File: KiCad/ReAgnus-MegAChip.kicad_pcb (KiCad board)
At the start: 4 copper layers, 78 x 49 mm, 24 parts, among them J1 Conn_01x03, J3 Conn_02x01, J4 Conn_01x01, J5 Conn_01x01, J6 Conn_01x01, J7 Conn_01x01, U1 PLCC-84-Plug, U2 LM1117-3.3, U3 SN74CBTD16210, U4 SN74CBTD16210, U5 SN74CBTD16210, U6 SN74CBTD16210, U7 GW1N-UV9LQ144, U8 74LVC1G07, U9 Agnus_TH_plug_pins

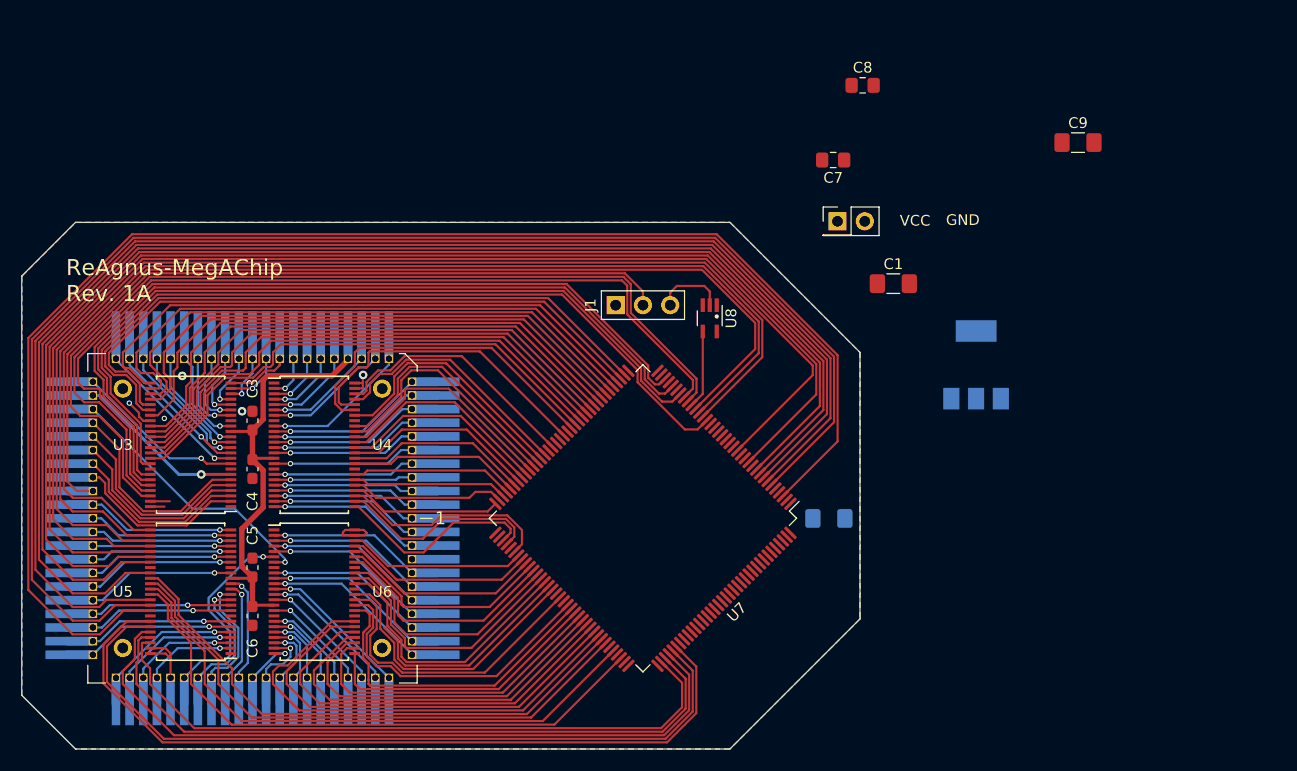
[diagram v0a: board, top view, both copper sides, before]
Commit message: added pull-up resistors on PAL/NTSC-line, added JTAG-header
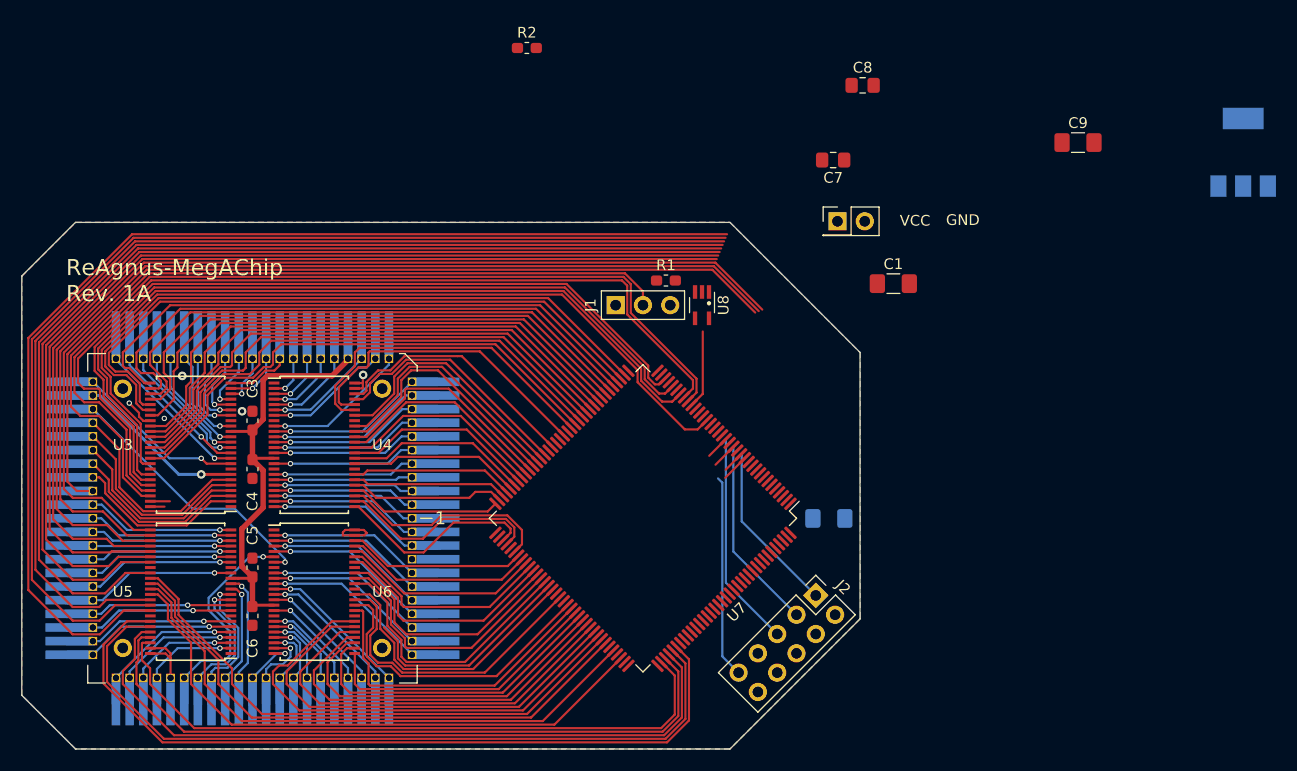
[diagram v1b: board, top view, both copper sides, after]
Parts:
- added J2: Conn_02x05_Odd_Even, Connector_PinHeader_2.54mm:PinHeader_2x05_P2.54mm_Vertical, F.Cu at (191.2, 122.0)
- added R1: 10k, Resistor_SMD:R_0603_1608Metric_Pad1.05x0.95mm_HandSolder, F.Cu at (177.2, 92.7)
- added R2: 10k, Resistor_SMD:R_0603_1608Metric_Pad1.05x0.95mm_HandSolder, F.Cu at (164.3, 71.1)
- moved U2 31.8 mm to (230.9, 80.8)
- moved U8 1.42 mm to (180.6, 95.0)
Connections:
- net Net-(J1-Pad3) renamed PAL_NTSC
- net Net-(U7-Pad11) renamed GCLKT_7
- net Net-(U7-Pad123) renamed GCLKT_1
- net Net-(U7-Pad143) renamed MODE1
- net Net-(U7-Pad144) renamed MODE0
- net Net-(U7-Pad20) renamed RECONFIG_N
- net Net-(U7-Pad21) renamed DONE
- net Net-(U7-Pad22) renamed READY
- net Net-(U7-Pad56) renamed GCLKT_5
- net Net-(U7-Pad58) renamed GCLKT_4
- J1 pad 2: GND|NTSC -> GND|PAL_NTSC
- U7 pad 13: Net-(U7-Pad13) -> TMS
- U7 pad 14: Net-(U7-Pad14) -> TCK
- U7 pad 16: Net-(U7-Pad16) -> TDI
- U7 pad 18: Net-(U7-Pad18) -> TDO
- U8 pad 4: GND|NTSC_3V3 -> PAL_NTSC_3V3
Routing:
- net LDS|UDS_3V3: track 136.6 -> 106.4 mm
- net DRA8|LDS_3V3: track 133.0 -> 104.0 mm
- net DRA8|DRA7_3V3: track 129.9 -> 101.6 mm
- net DRA7|DRA6_3V3: track 127.5 -> 100.0 mm
- net DRA6|DRA5_3V3: track 124.6 -> 97.8 mm
- net DRA5|DRA4_3V3: track 121.4 -> 95.4 mm
- net DRA4|DRA3_3V3: track 118.0 -> 93.0 mm
- net DRA3|DRA2_3V3: track 115.0 -> 91.2 mm
- net TDO: track 0.00 -> 22.3 mm
- net TMS: track 0.00 -> 21.5 mm
- net TDI: track 0.00 -> 20.4 mm
- net TCK: track 0.00 -> 18.0 mm
- net DRA2|DRA1_3V3: track 107.2 -> 95.6 mm
- net DRA1|DRA0_3V3: track 104.7 -> 93.5 mm
- net DRA0_3V3|GND: track 102.2 -> 91.5 mm
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
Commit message: more routing and placing components
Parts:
- removed the C9 at (215.6, 79.9)
- removed J1: Conn_01x03, Connector_PinHeader_2.54mm:PinHeader_1x03_P2.54mm_Vertical
- removed the R1 at (177.2, 92.7)
- added C10: 0.01uF, Capacitor_SMD:C_0603_1608Metric_Pad1.05x0.95mm_HandSolder, F.Cu at (169.2, 99.2)
- added C8: C_Small, Capacitor_SMD:C_1210_3225Metric_Pad1.42x2.65mm_HandSolder, B.Cu at (162.5, 82.3)
- added U10: AS4C4M16SA, Package_SO:TSOP-II-54_22.2x10.16mm_P0.8mm, B.Cu at (175.1, 114.8)
- C2, U2: moved to F.Cu
- moved U2 56.6 mm to (176.4, 95.9), turned to 180 degrees
- moved R1 34.1 mm to (193.2, 89.2)
- moved C2 31.1 mm to (168.5, 94.9), turned to 0 degrees
- moved C7 28.4 mm to (169.1, 97.2)
- moved U8 26.3 mm to (202.5, 80.5)
- moved J3 16.5 mm to (192.6, 103.7), turned to 270 degrees
- moved C1 15.8 mm to (183.4, 97.9), turned to 90 degrees
- moved C9 13.2 mm to (184.7, 82.0), turned to 270 degrees
- renumbered C8 to C9, R2 to R1
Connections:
- net PAL_NTSC_3V3 renamed nNTSC_8372_3V3
- U1 pad 41: GND|NTSC -> GND|nNTSC_8372
- U8 pad 2: PAL_NTSC -> GND|nNTSC_8372
- U9 pad 41: GND|NTSC -> GND|nNTSC_8372
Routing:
- net GND|nNTSC_8372: track 0.00 -> 90.3 mm
- net 3V3: track 0.00 -> 77.9 mm, vias 0 -> 5
- net GND|NTSC: track 75.7 -> 0.00 mm
- net VCC: track 42.6 -> 97.8 mm
- net TDO: track 22.3 -> 2.19 mm
- net TMS: track 21.5 -> 2.59 mm
- net TDI: track 20.4 -> 2.36 mm
- net DRA8|LDS_3V3: track 104.0 -> 121.8 mm
- net LDS|UDS_3V3: track 106.4 -> 124.1 mm
- net DRA8|DRA7_3V3: track 101.6 -> 118.1 mm
- net DRA7|DRA6_3V3: track 100.0 -> 116.1 mm
- net TCK: track 18.0 -> 2.03 mm
- net DRA6|DRA5_3V3: track 97.8 -> 113.5 mm
- net DRA5|DRA4_3V3: track 95.4 -> 110.5 mm
- net DRA4|DRA3_3V3: track 93.0 -> 107.7 mm
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
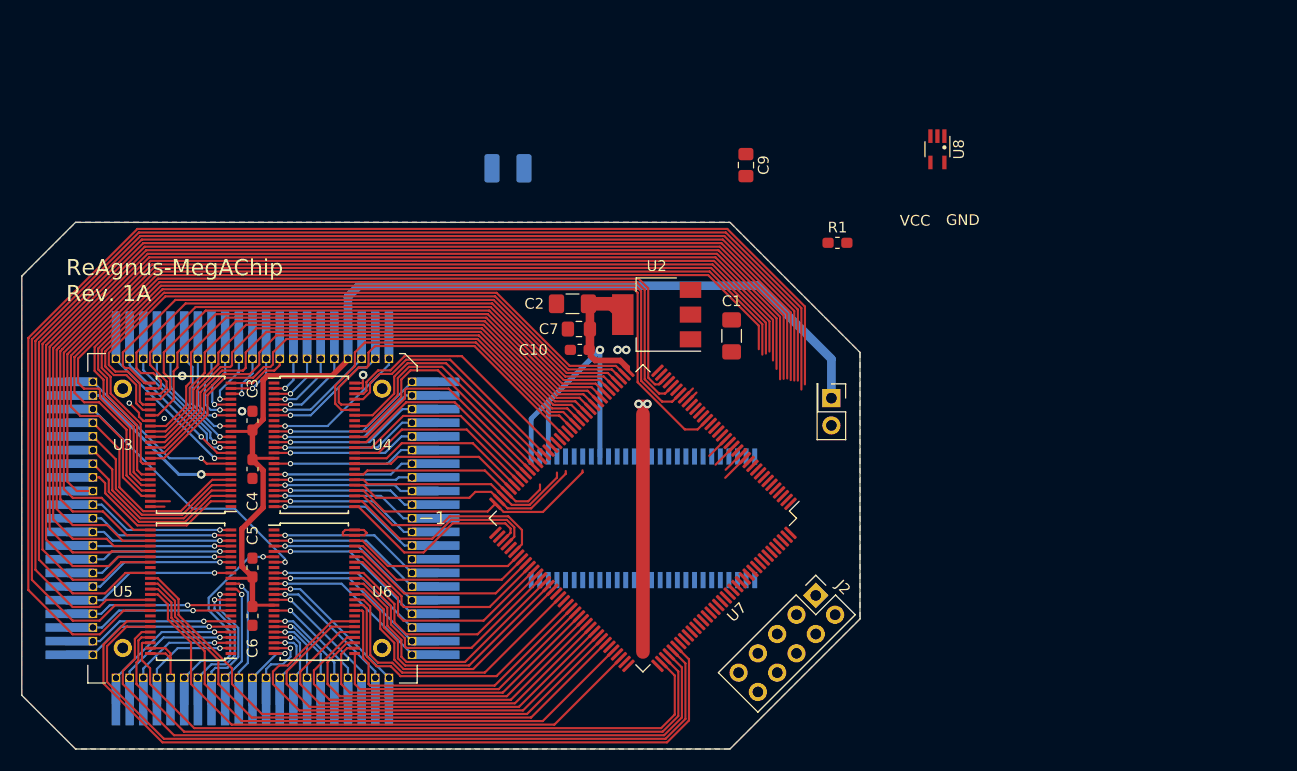
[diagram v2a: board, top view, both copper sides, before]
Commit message: fixed routing for VCC to voltage regulator, placed two-pin header for VCC/GND and more routing
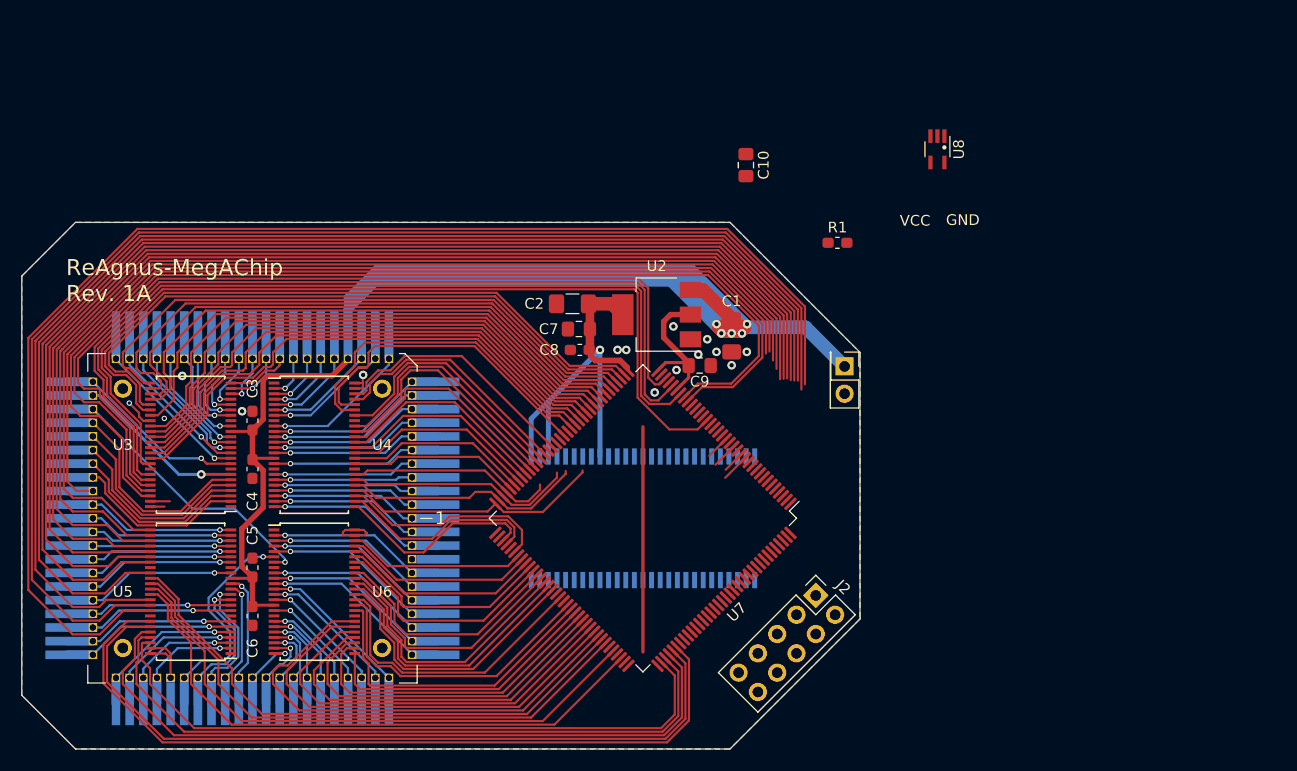
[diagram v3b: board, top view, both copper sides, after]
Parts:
- removed the C8 at (162.5, 82.3)
- added C9: 0.1uF, Capacitor_SMD:C_0805_2012Metric_Pad1.15x1.40mm_HandSolder, F.Cu at (180.4, 100.6)
- moved J3 3.20 mm to (193.9, 100.7)
- renumbered C9 to C10, C10 to C8
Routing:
- net VCC: track 97.8 -> 202.6 mm, vias 0 -> 5
- net 3V3: track 77.9 -> 87.6 mm, vias 5 -> 3
- net CCK|CCKQ_3V3: track 88.8 -> 96.8 mm
- net 14M|CCK_3V3: track 91.2 -> 98.9 mm
- net 7M|CDAC_3V3: track 80.7 -> 82.1 mm
- net CDAC|XCLKEN_3V3: track 80.4 -> 81.4 mm
- net 28M_3V3: track 82.1 -> 83.0 mm
- net GND: vias 5 -> 13

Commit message: more routing and placing components
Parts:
- removed R1: 10k, Resistor_SMD:R_0603_1608Metric_Pad1.05x0.95mm_HandSolder
- added C11: 0.01uF, Capacitor_SMD:C_0603_1608Metric_Pad1.05x0.95mm_HandSolder, F.Cu at (188.3, 107.7)
- added RN1: R_Pack04, Agnus:RESCAF80P320X160X60-8N, F.Cu at (185.5, 104.8)
- moved U8 25.1 mm to (187.4, 100.5)
- moved C10 22.4 mm to (189.4, 103.9), turned to 90 degrees
- moved C9 0.31 mm to (180.6, 100.4)
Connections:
- C10 pad 1: GND -> 3V3
- C10 pad 2: 3V3 -> GND
- U7 pad 24: DRA2|DRA1_3V3 -> nNTSC_8372_3V3
- U7 pad 25: DRA1|DRA0_3V3 -> DRA2|DRA1_3V3
- U7 pad 26: DRA0_3V3|GND -> DRA1|DRA0_3V3
- U7 pad 27: GND|NTSC_3V3 -> DRA0_3V3|GND
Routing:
- net 3V3: track 87.6 -> 177.4 mm, vias 3 -> 8
- net DRA3|DRA2_3V3: track 105.5 -> 120.2 mm
- net DRA8|DRA7_3V3: track 118.1 -> 132.3 mm
- net DRA4|DRA3_3V3: track 107.7 -> 121.8 mm
- net DRA7|DRA6_3V3: track 116.1 -> 130.1 mm
- net LDS|UDS_3V3: track 124.1 -> 138.0 mm
- net DRA6|DRA5_3V3: track 113.5 -> 127.3 mm
- net DRA5|DRA4_3V3: track 110.5 -> 124.3 mm
- net DRA8|LDS_3V3: track 121.8 -> 135.3 mm
- net DRA0_3V3|GND: track 96.4 -> 108.5 mm
- net DRA1|DRA0_3V3: track 99.4 -> 110.9 mm
- net DRA2|DRA1_3V3: track 102.4 -> 113.3 mm
- net nNTSC_8372_3V3: track 0.00 -> 8.12 mm
- net GND: track 20.3 -> 25.9 mm, vias 13 -> 19
- net RECONFIG_N: track 0.00 -> 4.31 mm
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
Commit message: more routing and placing components
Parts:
- added C11: 0.1uF, Capacitor_SMD:C_0805_2012Metric_Pad1.15x1.40mm_HandSolder, F.Cu at (192.7, 114.4)
- added C12: 0.1uF, Capacitor_SMD:C_0805_2012Metric_Pad1.15x1.40mm_HandSolder, F.Cu at (192.7, 112.5)
- added RN2: R_Pack04, Agnus:RESCAF80P320X160X60-8N, F.Cu at (192.7, 118.2)
- moved J2 1.48 mm to (190.5, 123.3)
- renumbered C11 to C15
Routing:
- net 3V3: track 177.4 -> 237.2 mm, vias 8 -> 10
- net TCK: track 2.03 -> 7.36 mm
- net MODE1: track 0.00 -> 3.89 mm
- net MODE0: track 0.00 -> 3.35 mm
- net GND: vias 19 -> 24

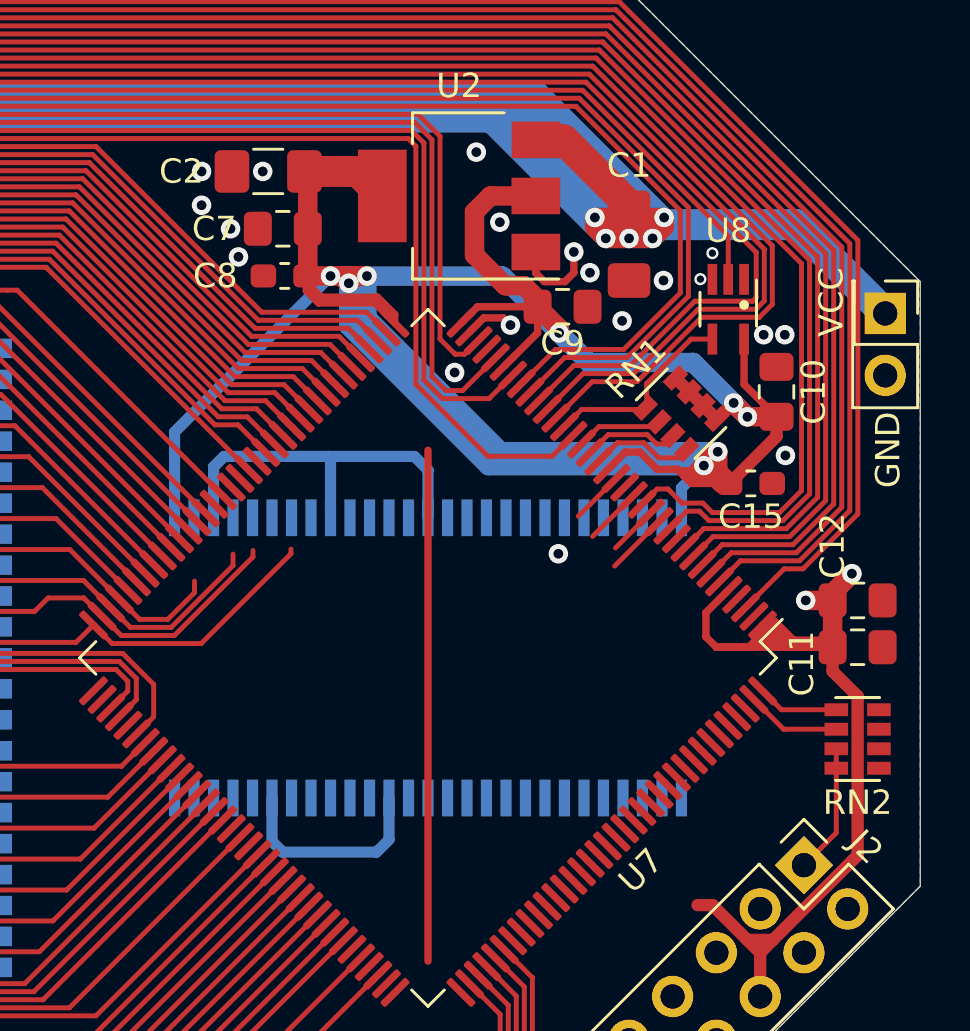
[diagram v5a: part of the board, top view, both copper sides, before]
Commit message: went to two layers, deleted inner layers GND and VCC
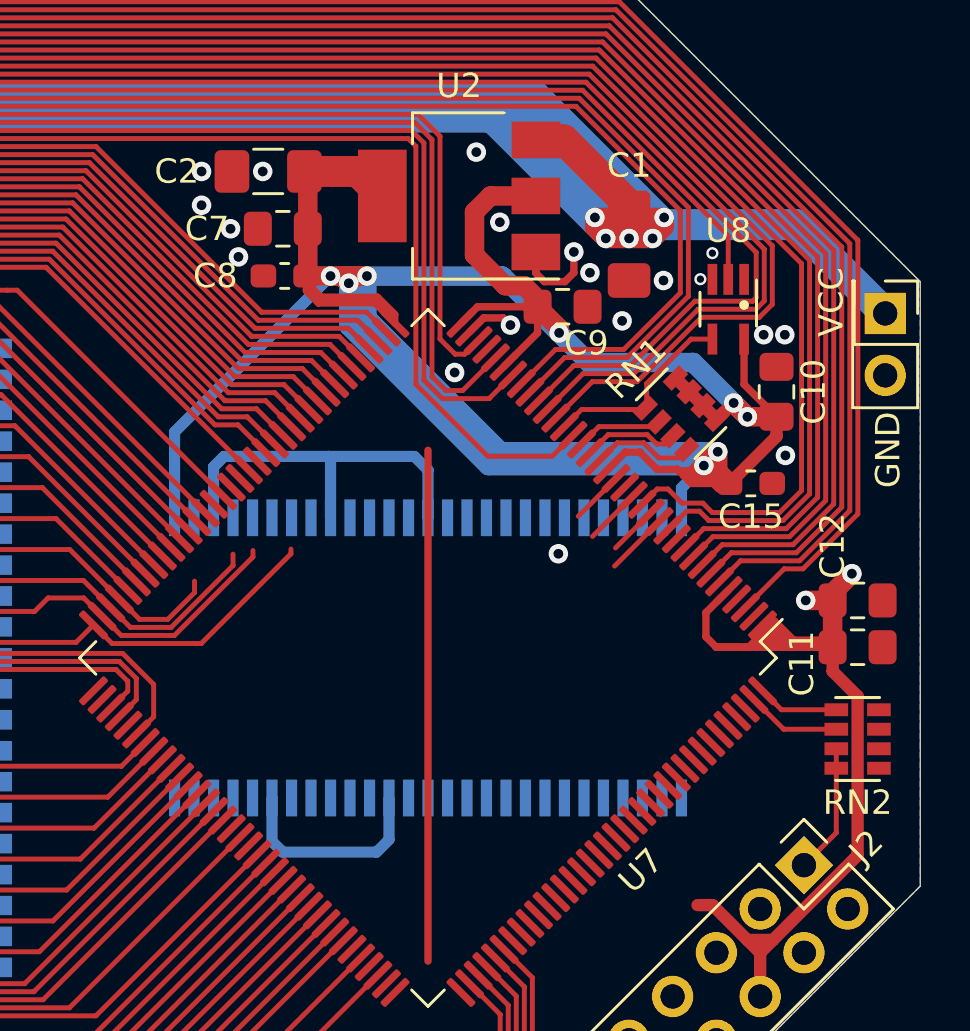
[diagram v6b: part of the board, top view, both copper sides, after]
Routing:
- removed copper zone on GND.Cu, net GND
- removed copper zone on VCC.Cu, net VCC
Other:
- copper layers 4 -> 2
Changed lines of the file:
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@@
   (general
     (thickness 1.6)
-    (drawings 16)
+    (drawings 15)
     (tracks 1561)
     (zones 0)
@@
   (layers
     (0 F.Cu signal)
-    (1 GND.Cu power)
-    (2 VCC.Cu power)
     (31 B.Cu signal)
     (32 B.Adhes user)
@@
   )
   (setup
-    (last_trace_width 0.127)
+    (last_trace_width 0.2032)
     (user_trace_width 0.127)
     (user_trace_width 0.1524)
@@
     (tags "capacitor handsolder")
     (attr smd)
-    (fp_text reference C9 (at 0 1.49352) (layer F.SilkS)
+    (fp_text reference C9 (at 0.97536 1.49352) (layer F.SilkS)
       (effects (font (size 1 1) (thickness 0.15)))
     )
@@
     (descr "Through hole straight pin header, 2x05, 2.54mm pitch, double rows")
     (tags "Through hole pin header THT 2x05 2.54mm double row")
-    (fp_text reference J2 (at 1.27 -2.33 135) (layer F.SilkS)
+    (fp_text reference J2 (at 1.27 -2.33 225) (layer F.SilkS)
       (effects (font (size 1 1) (thickness 0.15)))
     )
@@
     (tags "capacitor handsolder")
     (attr smd)
-    (fp_text reference C7 (at 2.81548 0) (layer F.SilkS)
+    (fp_text reference C7 (at 3.11012 0) (layer F.SilkS)
       (effects (font (size 1 1) (thickness 0.15)))
     )
@@
     (tags "capacitor handsolder")
     (attr smd)
-    (fp_text reference C2 (at -3.56202 0 180) (layer F.SilkS)
+    (fp_text reference C2 (at -3.75506 0 180) (layer F.SilkS)
       (effects (font (size 1 1) (thickness 0.15)))
     )
@@
   (gr_line (start 122.3 136.3) (end 117.3 131.3) (layer Edge.Cuts) (width 0.05))
   (gr_line (start 195.3 124.2) (end 183.2 136.3) (layer Edge.Cuts) (width 0.05))
-  (dimension 6.6 (width 0.15) (layer Dwgs.User)
-    (gr_text "6.600 mm" (at 156.9 127.6) (layer Dwgs.User)
-      (effects (font (size 1 1) (thickness 0.15)))
-    )
-    (feature1 (pts (xy 160.2 126.3) (xy 160.2 126.886421)))
-    (feature2 (pts (xy 153.6 126.3) (xy 153.6 126.886421)))
-    (crossbar (pts (xy 153.6 126.3) (xy 160.2 126.3)))
-    (arrow1a (pts (xy 160.2 126.3) (xy 159.073496 126.886421)))
-    (arrow1b (pts (xy 160.2 126.3) (xy 159.073496 125.713579)))
-    (arrow2a (pts (xy 153.6 126.3) (xy 154.726504 126.886421)))
-    (arrow2b (pts (xy 153.6 126.3) (xy 154.726504 125.713579)))
-  )
   (gr_line (start 195.3 99.4) (end 183.2 87.3) (layer Edge.Cuts) (width 0.05))
   (gr_line (start 122.3 87.3) (end 183.2 87.3) (layer Edge.Cuts) (width 0.05))
@@
       )
     )
-  )
-  (zone (net 2) (net_name GND) (layer GND.Cu) (hatch edge 0.508)
-    (connect_pads (clearance 0.1524))
-    (min_thickness 0.1524)
-    (fill yes (arc_segments 32) (thermal_gap 0.254) (thermal_bridge_width 0.508))
-    (polygon
-      (pts
-        (xy 117.3 131.3) (xy 117.3 92.3) (xy 122.3 87.3) (xy 183.2 87.3) (xy 195.3 99.4)
-        (xy 195.3 124.2) (xy 183.2 136.3) (xy 122.3 136.3)
-      )
-    )
-  )
-  (zone (net 1) (net_name VCC) (layer VCC.Cu) (hatch edge 0.508)
-    (connect_pads (clearance 0.1524))
-    (min_thickness 0.1524)
-    (fill yes (arc_segments 32) (thermal_gap 0.254) (thermal_bridge_width 0.508))
-    (polygon
-      (pts
-        (xy 117.3 131.3) (xy 117.3 92.3) (xy 122.3 87.3) (xy 183.2 87.3) (xy 195.3 99.4)
-        (xy 195.3 124.2) (xy 183.2 136.3) (xy 122.3 136.3)
-      )
-    )

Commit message: more routing and placing components
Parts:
- added C12: 0.1uF, Capacitor_SMD:C_0805_2012Metric_Pad1.15x1.40mm_HandSolder, F.Cu at (185.8, 123.7)
- added C14: 0.01uF, Capacitor_SMD:C_0805_2012Metric_Pad1.15x1.40mm_HandSolder, F.Cu at (173.4, 132.4)
- added C16: CP_Small, Capacitor_THT:CP_Radial_D5.0mm_P2.50mm, F.Cu at (162.6, 94.6)
- C13: renamed from C12; value 0.1uF -> 0.01uF
- C3, C4, C5: value C_Small -> 0.1uF
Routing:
- net VCC: track 202.6 -> 159.9 mm
- net 3V3: track 237.2 -> 248.0 mm
- net GND: vias 24 -> 27
